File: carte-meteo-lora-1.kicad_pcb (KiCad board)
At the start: 2 copper layers, 60 x 45 mm, 121 parts, among them J1 TC2030, J2 Conn_01x04, J3 Conn_01x04, J4 Conn_Coaxial, J5 USB_C_Receptacle_USB2.0_14P, J6 Solar_Cell, J7 Conn_01x02, J8 Battery_Cell, Q1 AO4882, Q2 AO4882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

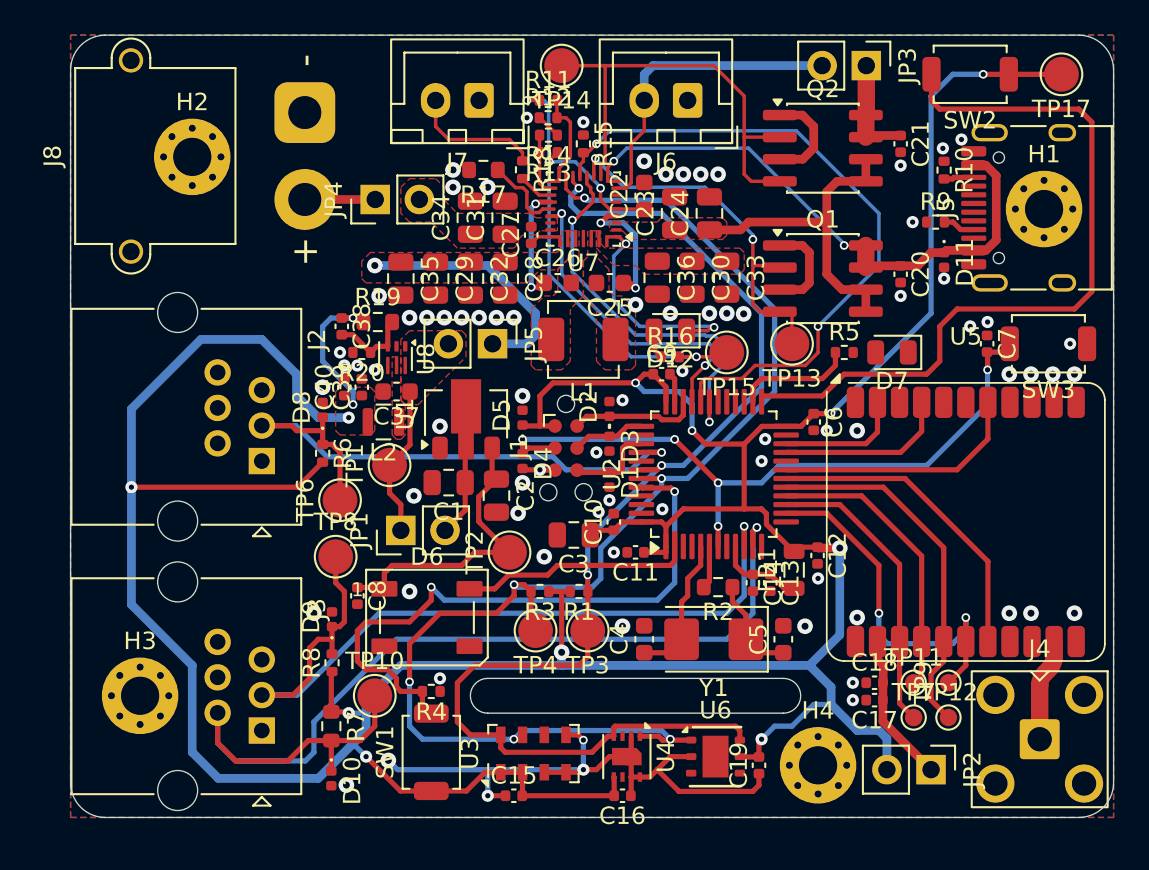
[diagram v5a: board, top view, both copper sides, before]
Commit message: pcb: add missing connections
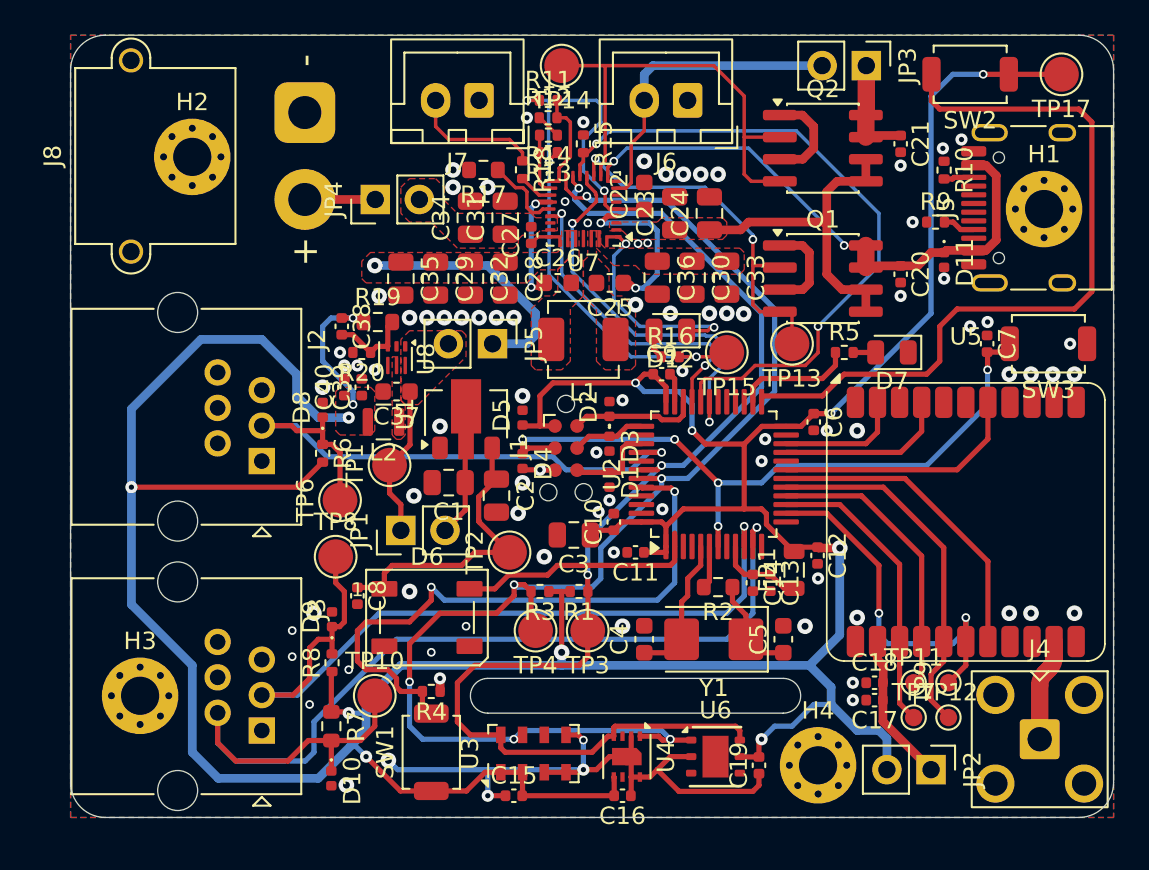
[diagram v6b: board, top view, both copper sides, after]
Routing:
- net +REGN: track 32.9 -> 38.2 mm
- net Net-(U7-BTST1): track 7.23 -> 9.41 mm
- net Net-(D7-A): track 0.00 -> 1.29 mm
- net GND: track 41.7 -> 42.5 mm, vias 76 -> 86
- net /SCL: track 70.8 -> 70.3 mm

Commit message: pcb: add stitching vias
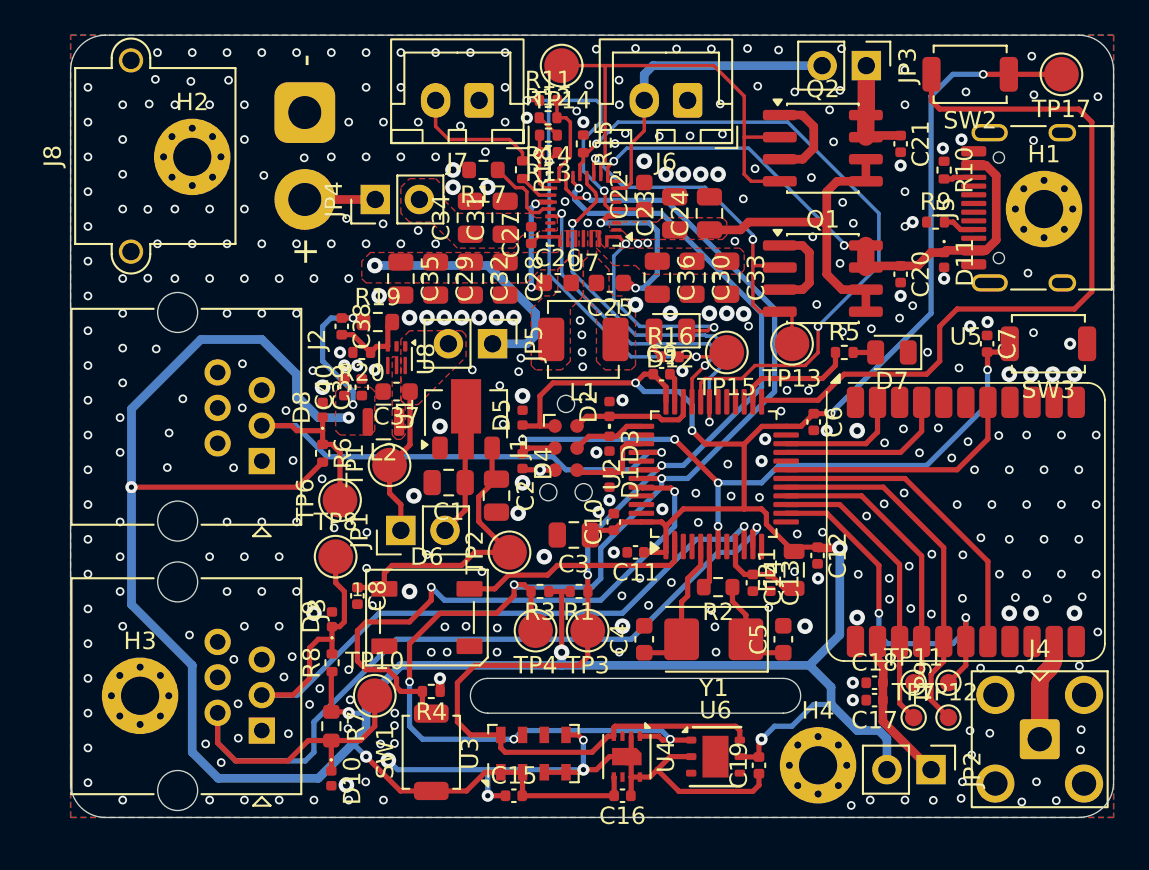
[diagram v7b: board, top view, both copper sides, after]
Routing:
- net /W_DIR: track 59.2 -> 56.6 mm
- net /WIND: track 48.0 -> 45.7 mm
- net /BOOT: track 35.7 -> 33.8 mm
- net GND: vias 86 -> 374
